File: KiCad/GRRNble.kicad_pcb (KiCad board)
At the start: 2 copper layers, 28 x 41 mm, 48 parts, among them J1 JST_SH_06, Q1 DMG3415U, Q2 BSS138, Q3 DMG3415U, SW1 SW_Push, SW2 SW_Push, SW3 SW_Push, U1 R5F100LJAFB, U2 BUZZER, U3 SSD1306, U4 MCP73831, U5 RN4020, U6 MCP1703A-3302_SOT23, Y1 32.768k

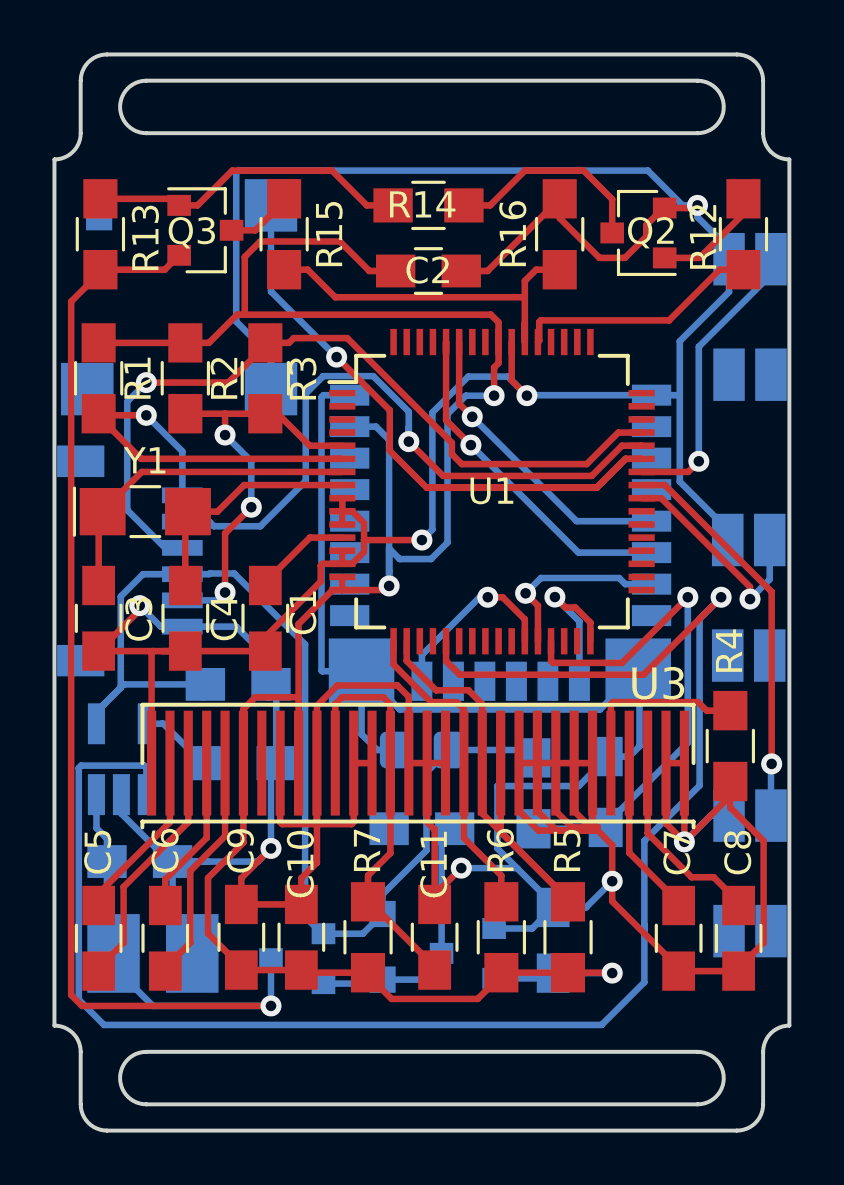
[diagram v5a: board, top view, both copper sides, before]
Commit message: change PCB layout
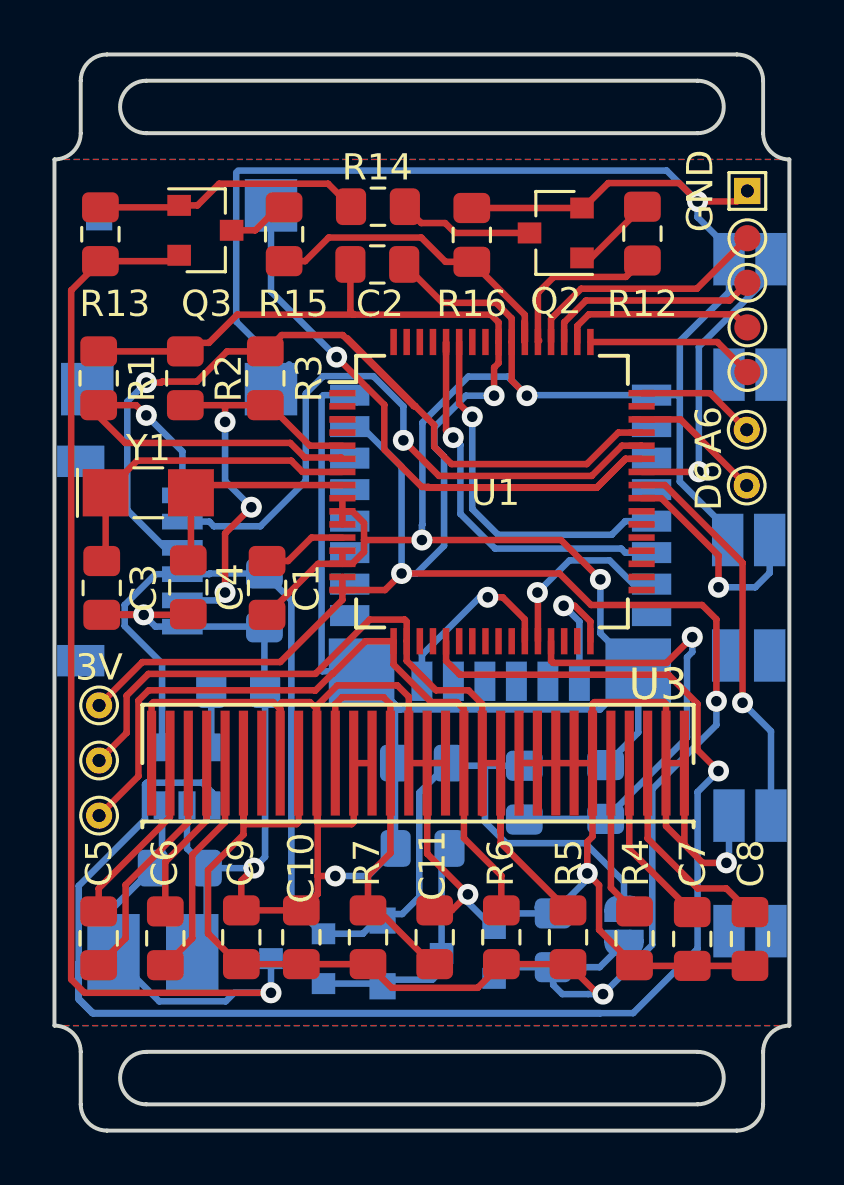
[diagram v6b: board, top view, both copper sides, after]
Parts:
- added 3V: +3V, TestPoint:TestPoint_THTPad_D1.0mm_Drill0.5mm, F.Cu at (97.0, 104.5)
- added A2: A2, TestPoint:TestPoint_Pad_D1.0mm, F.Cu at (121.7, 86.7)
- added A3: A3, TestPoint:TestPoint_Pad_D1.0mm, F.Cu at (121.7, 88.3)
- added A4: A4, TestPoint:TestPoint_Pad_D1.0mm, F.Cu at (121.7, 90.0)
- added A5: A5, TestPoint:TestPoint_Pad_D1.0mm, F.Cu at (121.7, 91.8)
- added A6: A6, TestPoint:TestPoint_THTPad_D1.0mm_Drill0.5mm, F.Cu at (121.6, 94.0)
- added D6: D6, TestPoint:TestPoint_THTPad_D1.0mm_Drill0.5mm, F.Cu at (121.6, 96.1)
- added GND: GND, TestPoint:TestPoint_THTPad_1.0x1.0mm_Drill0.5mm, F.Cu at (121.7, 84.8)
- added JP1: Jumper_NO_Small, Jumper:SolderJumper-2_P1.3mm_Open_RoundedPad1.0x1.5mm, B.Cu at (117.0, 112.8)
- added SCL: SCL, TestPoint:TestPoint_THTPad_D1.0mm_Drill0.5mm, F.Cu at (97.0, 108.7)
- added SDA: SDA, TestPoint:TestPoint_THTPad_D1.0mm_Drill0.5mm, F.Cu at (97.0, 106.5)
- C1, C10, C11, C12, C13, C15, C16, C2, C3, C4, C5, C6, C7, C8, C9: footprint Capacitors_SMD:C_0805_HandSoldering -> Capacitor_SMD:C_0805_2012Metric_Pad1.15x1.40mm_HandSolder
- D1: footprint Diodes_SMD:D_SOD-323_HandSoldering -> Diode_SMD:D_SOD-323_HandSoldering
- Q1, Q2, Q3: footprint TO_SOT_Packages_SMD:SOT-23 -> Package_TO_SOT_SMD:SOT-23
- R1, R10, R12, R13, R14, R15, R16, R2, R3, R4, R5, R6, R7, R8, R9: footprint Resistors_SMD:R_0805_HandSoldering -> Resistor_SMD:R_0805_2012Metric_Pad1.15x1.40mm_HandSolder
- U1: footprint Housings_QFP:LQFP-64_10x10mm_Pitch0.5mm -> Package_QFP:LQFP-64_10x10mm_P0.5mm
- U4: value MCP73831 -> MCP73831-2-OT; footprint TO_SOT_Packages_SMD:SOT-23-5_HandSoldering -> Package_TO_SOT_SMD:SOT-23-5
- Y1: footprint Crystals:Crystal_SMD_G8-2pin_3.2x1.5mm_HandSoldering -> Crystal:Crystal_SMD_G8-2Pin_3.2x1.5mm_HandSoldering
- moved R4 8.18 mm to (117.3, 113.3)
- moved R12 3.85 mm to (117.7, 86.5)
- moved C12 3.35 mm to (103.2, 100.5), turned to 270 degrees
- moved R16 3.35 mm to (111.2, 86.5)
- moved Q2 3.15 mm to (114.3, 86.5)
- moved R8 2.80 mm to (102.2, 103.8)
- moved U4 2.58 mm to (100.3, 107.2)
- moved G*** 2.37 mm to (104.8, 107.8), turned to 270 degrees
- moved C2 1.97 mm to (107.5, 87.7)
- moved R14 1.93 mm to (107.6, 85.5)
- moved C13 1.55 mm to (100.0, 110.7)
- moved C4 1.19 mm to (100.3, 100.0)
- moved C3 1.16 mm to (97.0, 100.0)
- moved C1 1.16 mm to (103.3, 100.0)
- moved C15 0.75 mm to (109.3, 109.9)
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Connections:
- J1 pad M1: Net-(J1-PadM1) -> (no net)
- J1 pad M2: Net-(J1-PadM2) -> (no net)
- U1 pad 1: Net-(U1-Pad1) -> (no net)
- U1 pad 19: Net-(U1-Pad19) -> (no net)
- U1 pad 2: Net-(U1-Pad2) -> (no net)
- U1 pad 20: Net-(U1-Pad20) -> (no net)
- U1 pad 22: Net-(U1-Pad22) -> (no net)
- U1 pad 23: Net-(U1-Pad23) -> (no net)
- U1 pad 24: Net-(U1-Pad24) -> (no net)
- U1 pad 25: Net-(U1-Pad25) -> (no net)
- U1 pad 26: Net-(U1-Pad26) -> (no net)
- U1 pad 3: Net-(U1-Pad3) -> (no net)
- U1 pad 30: Net-(U1-Pad30) -> (no net)
- U1 pad 31: Net-(U1-Pad31) -> (no net)
- U1 pad 33: Net-(U1-Pad33) -> (no net)
- U1 pad 34: Net-(U1-Pad34) -> (no net)
- U1 pad 35: Net-(U1-Pad35) -> (no net)
- U1 pad 36: Net-(U1-Pad36) -> (no net)
- U1 pad 37: Net-(U1-Pad37) -> (no net)
- U1 pad 38: Net-(U1-Pad38) -> (no net)
- U1 pad 39: Net-(U1-Pad39) -> (no net)
- U1 pad 4: Net-(U1-Pad4) -> (no net)
- U1 pad 46: Net-(U1-Pad46) -> D6
- U1 pad 47: Net-(U1-Pad47) -> (no net)
- U1 pad 48: Net-(U1-Pad48) -> A6
- U1 pad 49: Net-(U1-Pad49) -> A5
- U1 pad 50: Net-(U1-Pad50) -> A4
- U1 pad 51: Net-(U1-Pad51) -> A3
- U1 pad 52: Net-(U1-Pad52) -> A2
- U1 pad 57: Net-(U1-Pad57) -> (no net)
- U1 pad 58: Net-(U1-Pad58) -> (no net)
- U1 pad 61: Net-(U1-Pad61) -> (no net)
- U1 pad 62: Net-(U1-Pad62) -> (no net)
- U1 pad 63: Net-(U1-Pad63) -> (no net)
- U1 pad 64: Net-(U1-Pad64) -> (no net)
- U2 pad 3: Net-(U2-Pad3) -> (no net)
- U2 pad 4: Net-(U2-Pad4) -> (no net)
- U3 pad 7: Net-(U3-Pad7) -> (no net)
- U5 pad 11: Net-(U5-Pad11) -> (no net)
- U5 pad 12: Net-(U5-Pad12) -> (no net)
- U5 pad 13: Net-(U5-Pad13) -> (no net)
- U5 pad 14: Net-(U5-Pad14) -> (no net)
- U5 pad 17: Net-(U5-Pad17) -> (no net)
- U5 pad 18: Net-(U5-Pad18) -> (no net)
- U5 pad 19: Net-(U5-Pad19) -> (no net)
- U5 pad 2: Net-(U5-Pad2) -> (no net)
- U5 pad 20: Net-(U5-Pad20) -> (no net)
- U5 pad 21: Net-(U5-Pad21) -> (no net)
- U5 pad 22: Net-(U5-Pad22) -> (no net)
- U5 pad 3: Net-(U5-Pad3) -> (no net)
- U5 pad 4: Net-(U5-Pad4) -> (no net)
- U5 pad 8: Net-(U5-Pad8) -> (no net)
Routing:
- net +3V3: track 88.8 -> 121.0 mm, vias 3 -> 4
- net STAT: track 63.9 -> 79.7 mm
- net SCL: track 12.2 -> 27.9 mm
- net SDA: track 21.3 -> 35.9 mm
- net A2: track 0.00 -> 9.64 mm
- net A3: track 0.00 -> 8.35 mm
- net A4: track 0.00 -> 7.48 mm
- net A5: track 0.00 -> 6.45 mm
- net Net-(C12-Pad1): track 43.2 -> 49.0 mm
- net D6: track 0.00 -> 5.05 mm
- net A6: track 0.00 -> 4.58 mm
- net TXD: track 30.2 -> 34.3 mm
- net BATT_ENABLE: track 9.39 -> 6.44 mm
- net Net-(Q2-Pad3): track 7.94 -> 5.16 mm
- net D8/RXD: track 11.5 -> 14.0 mm
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- added copper zone on B.Cu, net GND
- added copper zone on F.Cu, net GND
